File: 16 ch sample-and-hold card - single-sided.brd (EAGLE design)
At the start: 66 x 32.7 mm, 85 parts, among them IC1 MAX306CWI, IC2 TL074D, IC3 TL074D, IC4 TL074D, IC5 TL074D

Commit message: Almost finished, trying to reroute address lines
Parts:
- moved C1 0.32 mm to (26.0, 28.9)
- moved C10 0.32 mm to (48.3, 23.2)
- moved C11 0.32 mm to (45.7, 23.2)
- moved C2 0.32 mm to (19.4, 28.9)
- moved C22 0.32 mm to (10.2, 23.2)
- moved C23 0.32 mm to (7.62, 23.2)
- moved C24 0.32 mm to (5.08, 23.2)
- moved C25 0.32 mm to (2.54, 23.2)
- moved C26 0.32 mm to (20.3, 23.2)
- moved C27 0.32 mm to (17.8, 23.2)
- moved C28 0.32 mm to (15.2, 23.2)
- moved C29 0.32 mm to (12.7, 23.2)
- moved C3 0.32 mm to (14.0, 28.9)
- moved C4 0.32 mm to (63.5, 23.2)
- moved C40 0.32 mm to (23.5, 28.9)
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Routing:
- net +15V: track 109.0 -> 116.0 mm
- net AGND: track 213.0 -> 216.3 mm
- net IN28: track 48.3 -> 46.8 mm
- net N$4: track 10.3 -> 11.7 mm
- net -15V: track 155.0 -> 156.3 mm
- net OUT0: track 27.3 -> 26.0 mm
- net A3: track 42.5 -> 43.7 mm
- net OUT16: track 18.4 -> 17.3 mm
- net IN6: track 40.9 -> 39.9 mm
- net IN4: track 46.4 -> 45.4 mm
- net IN3: track 48.1 -> 47.0 mm
- net A1: track 51.4 -> 52.3 mm
- net IN1: track 48.2 -> 47.2 mm
- net A2: track 49.5 -> 50.4 mm
- net OUT24: track 18.9 -> 18.1 mm
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- added copper zone on layer 16, net DGND
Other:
- board size 66 x 32.7 mm -> 66 x 32.1 mm
- board text added: "+15v"
- board text added: "-15v"
- board text added: "1"
- board text added: "10n"
- board text added: "16ch sample & hold"
- board text added: "4"
- board text added: "4V&B"
- board text added: "9"
- board text added: "AGND"
- board text added: "Addr"
- board text added: "DAC in"
- board text added: "DGND"
- board text added: "EN"
- board text added: "Outputs"
- board text added: "XDSH"
- board text added: "v1.0"

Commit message: Rerouted address lines
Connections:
- net A0: now also U$1.5; no longer U$1.3
- net A2: now also U$1.3; no longer U$1.5
- net A3: now also U$1.2; no longer U$1.6
- net EN: now also U$1.6; no longer U$1.2
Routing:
- net A1: track 52.3 -> 56.3 mm
- net A2: track 50.4 -> 54.1 mm
- net A3: track 43.7 -> 46.8 mm
- net EN: track 54.9 -> 57.7 mm
- net A0: track 54.1 -> 55.9 mm
- net AGND: track 216.3 -> 214.7 mm

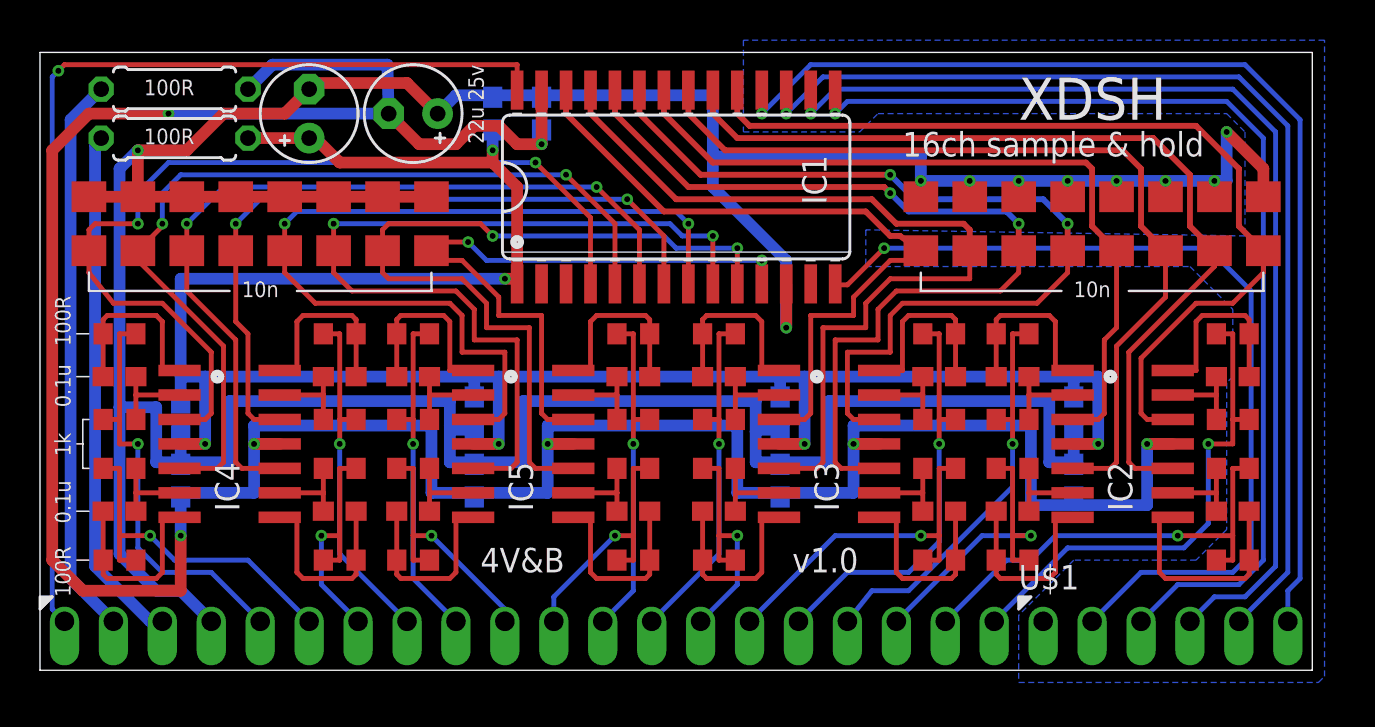
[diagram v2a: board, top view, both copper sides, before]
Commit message: Tweaked cap positions
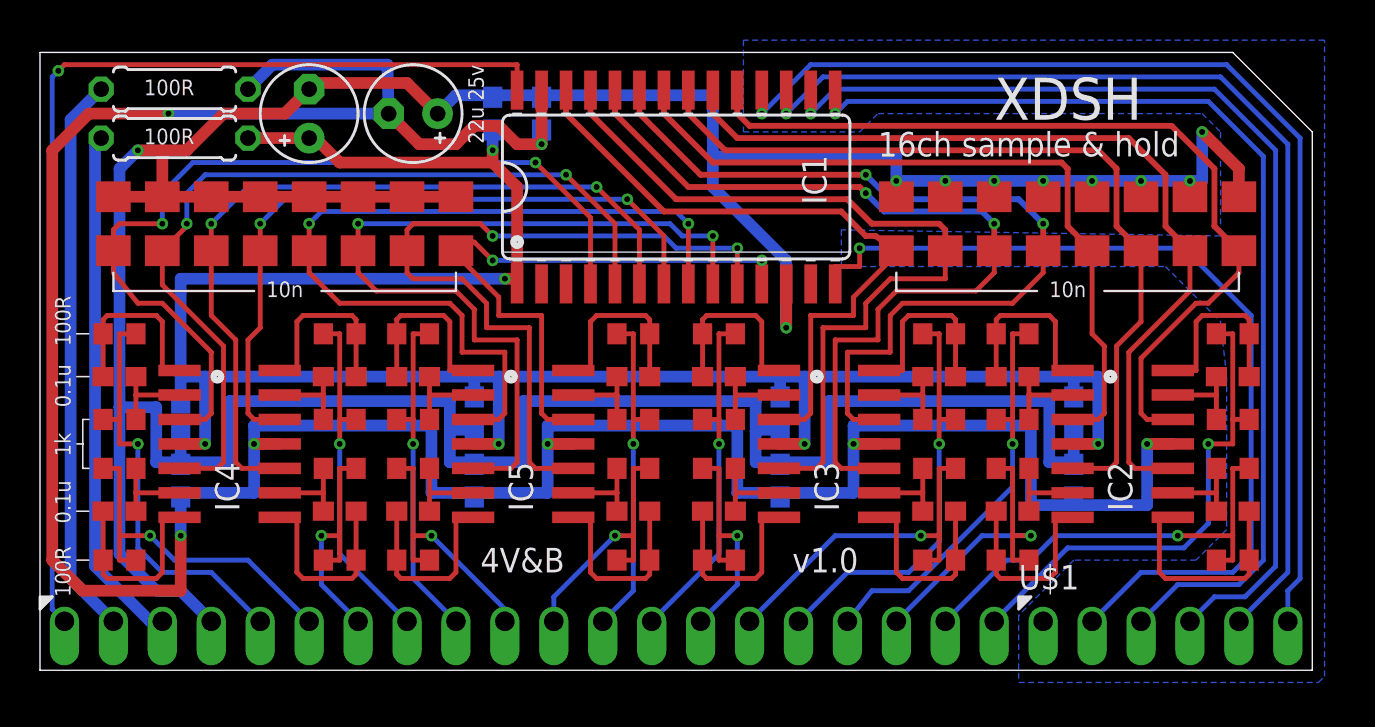
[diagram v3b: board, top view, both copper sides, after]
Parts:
- moved C4 1.27 mm to (62.2, 23.2)
- moved C5 1.27 mm to (59.7, 23.2)
- moved C6 1.27 mm to (57.1, 23.2)
- moved C7 1.27 mm to (54.6, 23.2)
- moved C8 1.27 mm to (52.1, 23.2)
- moved C28 1.27 mm to (16.5, 23.2)
- moved C29 1.27 mm to (14.0, 23.2)
- moved C23 1.27 mm to (8.89, 23.2)
- moved C25 1.27 mm to (3.81, 23.2)
- moved C22 1.27 mm to (11.4, 23.2)
- moved C24 1.27 mm to (6.35, 23.2)
- moved C26 1.27 mm to (21.6, 23.2)
- moved C27 1.27 mm to (19.1, 23.2)
- moved C10 1.27 mm to (47.0, 23.2)
- moved C11 1.27 mm to (44.5, 23.2)
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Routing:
- net IN9: track 47.6 -> 45.0 mm
- net IN20: track 45.6 -> 43.1 mm
- net IN19: track 42.1 -> 39.6 mm
- net IN22: track 46.4 -> 43.8 mm
- net IN1: track 47.2 -> 44.6 mm
- net IN30: track 48.4 -> 45.8 mm
- net IN12: track 44.8 -> 42.2 mm
- net IN11: track 47.7 -> 45.2 mm
- net IN14: track 37.3 -> 34.8 mm
- net IN17: track 33.7 -> 31.6 mm
- net IN3: track 47.0 -> 45.2 mm
- net IN4: track 45.4 -> 43.6 mm
- net IN28: track 46.8 -> 45.0 mm
- net IN27: track 43.9 -> 42.1 mm
- net IN6: track 39.9 -> 38.6 mm
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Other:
- outline, holes or cut-outs redrawn
